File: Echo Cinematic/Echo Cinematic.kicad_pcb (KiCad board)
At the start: 4 copper layers, 57.9 x 111.7 mm, 124 parts, among them J1 IDC, J11 SYM_Arrow45_Tiny, J12 SYM_Arrow45_Tiny, J13 SYM_Arrow45_Tiny, J14 SYM_Arrow45_Tiny, J15 SYM_Arrow45_Tiny, J16 Input R, J2 Play • Rec, J4 Tap • Clock, J5 AUDIO OUT L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

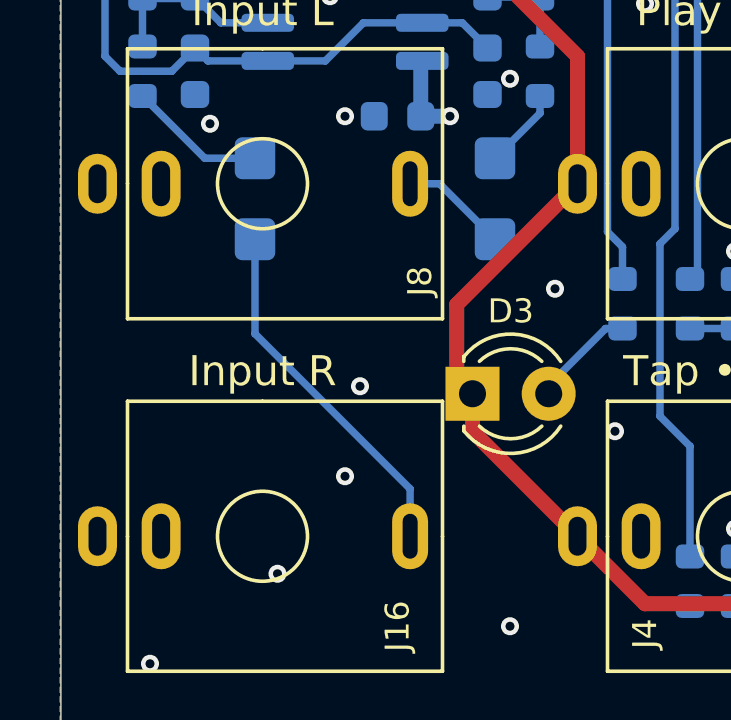
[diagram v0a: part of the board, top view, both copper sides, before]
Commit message: Added input jack switching circuits, fab files updated and finalized.
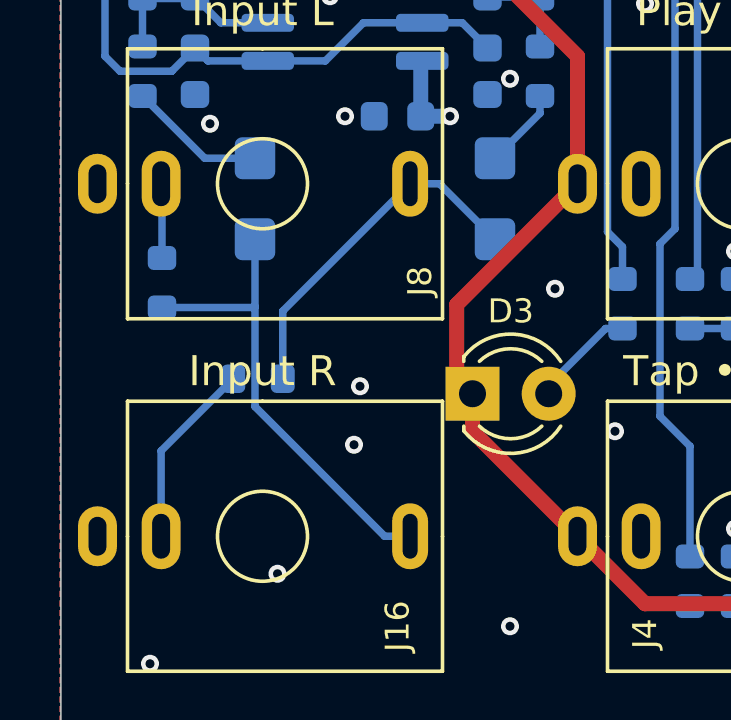
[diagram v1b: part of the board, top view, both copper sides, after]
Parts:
- added R51: 0R, Resistor_SMD:R_0603_1608Metric, B.Cu at (71.6, 137.0)
- added R52: 0R, Resistor_SMD:R_0603_1608Metric, B.Cu at (68.4, 133.8)
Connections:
- J16 pad TN: unconnected-(J16-PadTN) -> Net-(J16-PadTN)
- J8 pad TN: unconnected-(J8-PadTN) -> Net-(J8-PadTN)
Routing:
- net /AUDIO IN/AUDIO_IN_L: track 3.60 -> 11.9 mm
- net Net-(J16-PadTN): track 0.00 -> 6.25 mm
- net /AUDIO IN/AUDIO_IN_R: track 12.0 -> 15.6 mm
- net Net-(J8-PadTN): track 0.00 -> 2.49 mm
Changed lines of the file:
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@@
   (net 58 "unconnected-(J4-PadTN)")
   (net 59 "/AUDIO IN/AUDIO_IN_L")
-  (net 60 "unconnected-(J8-PadTN)")
+  (net 60 "Net-(J8-PadTN)")
   (net 61 "/AUDIO IN/AUDIO_IN_R")
-  (net 62 "unconnected-(J16-PadTN)")
+  (net 62 "Net-(J16-PadTN)")
   (net 63 "Net-(Q2-B)")
   (net 64 "Net-(Q2-C)")
@@
       (net 59 "/AUDIO IN/AUDIO_IN_L") (pintype "passive"))
     (pad "TN" thru_hole oval (at 0 3.38 270) (size 2.2 1.3) (drill oval 1.5 0.6) (layers "*.Cu" "*.Mask")
-      (net 60 "unconnected-(J8-PadTN)") (pintype "passive+no_connect"))
+      (net 60 "Net-(J8-PadTN)") (pintype "passive"))
     (model "${KIPRJMOD}/FOOTPRINTS.pretty/PJ301M-12 Thonkiconn v0.2.stp"
       (offset (xyz 0 0.7 0))
@@
       (net 61 "/AUDIO IN/AUDIO_IN_R") (pintype "passive"))
     (pad "TN" thru_hole oval (at 0 3.38 270) (size 2.2 1.3) (drill oval 1.5 0.6) (layers "*.Cu" "*.Mask")
-      (net 62 "unconnected-(J16-PadTN)") (pintype "passive+no_connect"))
+      (net 62 "Net-(J16-PadTN)") (pintype "passive"))
     (model "${KIPRJMOD}/FOOTPRINTS.pretty/PJ301M-12 Thonkiconn v0.2.stp"
       (offset (xyz 0 0.7 0))
@@
     )
   )
+  (footprint "Resistor_SMD:R_0603_1608Metric" (layer "B.Cu")
+    (at 68.4 133.8 -90)
+    (descr "Resistor SMD 0603 (1608 Metric), square (rectangular) end terminal, IPC_7351 nominal, (Body size source: IPC-SM-782 page 72, https://www.pcb-3d.com/wordpress/wp-content/uploads/ipc-sm-782a_amendment_1_and_2.pdf), generated with kicad-footprint-generator")
+    (tags "resistor")
+    (property "Sheetfile" "AUDIO IN.kicad_sch")
+    (property "Sheetname" "AUDIO IN")
+    (property "ki_description" "Resistor, small symbol")
+    (property "ki_keywords" "R resistor")
+    (attr smd)
+    (fp_text reference "R52" (at 0 1.43 90) (layer "B.SilkS")
+        (effects (font (size 0.8 0.8) (thickness 0.15)) (justify mirror))
+    )
+    (fp_text value "0R" (at 0 -1.43 90) (layer "B.Fab")
+        (effects (font (size 1 1) (thickness 0.15)) (justify mirror))
+    )
+    (fp_text user "${REFERENCE}" (at 0 0 90) (layer "B.Fab")
+        (effects (font (size 0.4 0.4) (thickness 0.06)) (justify mirror))
+    )
+    (fp_line (start -0.237258 -0.5225) (end 0.237258 -0.5225)
+      (stroke (width 0.12) (type solid)) (layer "B.SilkS"))
+    (fp_line (start -0.237258 0.5225) (end 0.237258 0.5225)
+      (stroke (width 0.12) (type solid)) (layer "B.SilkS"))
+    (fp_line (start -1.48 -0.73) (end -1.48 0.73)
+      (stroke (width 0.05) (type solid)) (layer "B.CrtYd"))
+    (fp_line (start -1.48 0.73) (end 1.48 0.73)
+      (stroke (width 0.05) (type solid)) (layer "B.CrtYd"))
+    (fp_line (start 1.48 -0.73) (end -1.48 -0.73)
+      (stroke (width 0.05) (type solid)) (layer "B.CrtYd"))
+    (fp_line (start 1.48 0.73) (end 1.48 -0.73)
+      (stroke (width 0.05) (type solid)) (layer "B.CrtYd"))
+    (fp_line (start -0.8 -0.4125) (end -0.8 0.4125)
+      (stroke (width 0.1) (type solid)) (layer "B.Fab"))
+    (fp_line (start -0.8 0.4125) (end 0.8 0.4125)
+      (stroke (width 0.1) (type solid)) (layer "B.Fab"))
+    (fp_line (start 0.8 -0.4125) (end -0.8 -0.4125)
+      (stroke (width 0.1) (type solid)) (layer "B.Fab"))
+    (fp_line (start 0.8 0.4125) (end 0.8 -0.4125)
+      (stroke (width 0.1) (type solid)) (layer "B.Fab"))
+    (pad "1" smd roundrect (at -0.825 0 270) (size 0.8 0.95) (layers "B.Cu" "B.Paste" "B.Mask") (roundrect_rratio 0.25)
+      (net 60 "Net-(J8-PadTN)") (pintype "passive"))
+    (pad "2" smd roundrect (at 0.825 0 270) (size 0.8 0.95) (layers "B.Cu" "B.Paste" "B.Mask") (roundrect_rratio 0.25)
+      (net 61 "/AUDIO IN/AUDIO_IN_R") (pintype "passive"))
+    (model "${KICAD6_3DMODEL_DIR}/Resistor_SMD.3dshapes/R_0603_1608Metric.wrl"
+      (offset (xyz 0 0 0))
+      (scale (xyz 1 1 1))
+      (rotate (xyz 0 0 0))
+    )
+  )
   (footprint "Capacitor_SMD:C_0603_1608Metric" (layer "B.Cu")
     (at 76.25 128.25 180)
@@
   )
   (footprint "Resistor_SMD:R_0603_1608Metric" (layer "B.Cu")
+    (at 71.6 137 180)
+    (descr "Resistor SMD 0603 (1608 Metric), square (rectangular) end terminal, IPC_7351 nominal, (Body size source: IPC-SM-782 page 72, https://www.pcb-3d.com/wordpress/wp-content/uploads/ipc-sm-782a_amendment_1_and_2.pdf), generated with kicad-footprint-generator")
+    (tags "resistor")
+    (property "Sheetfile" "AUDIO IN.kicad_sch")
+    (property "Sheetname" "AUDIO IN")
+    (property "ki_description" "Resistor, small symbol")
+    (property "ki_keywords" "R resistor")
+    (attr smd)
+    (fp_text reference "R51" (at 0 1.43) (layer "B.SilkS")
+        (effects (font (size 0.8 0.8) (thickness 0.15)) (justify mirror))
+    )
+    (fp_text value "0R" (at 0 -1.43) (layer "B.Fab")
+        (effects (font (size 1 1) (thickness 0.15)) (justify mirror))
+    )
+    (fp_text user "${REFERENCE}" (at 0 0) (layer "B.Fab")
+        (effects (font (size 0.4 0.4) (thickness 0.06)) (justify mirror))
+    )
+    (fp_line (start -0.237258 -0.5225) (end 0.237258 -0.5225)
+      (stroke (width 0.12) (type solid)) (layer "B.SilkS"))
+    (fp_line (start -0.237258 0.5225) (end 0.237258 0.5225)
+      (stroke (width 0.12) (type solid)) (layer "B.SilkS"))
+    (fp_line (start -1.48 -0.73) (end -1.48 0.73)
+      (stroke (width 0.05) (type solid)) (layer "B.CrtYd"))
+    (fp_line (start -1.48 0.73) (end 1.48 0.73)
+      (stroke (width 0.05) (type solid)) (layer "B.CrtYd"))
+    (fp_line (start 1.48 -0.73) (end -1.48 -0.73)
+      (stroke (width 0.05) (type solid)) (layer "B.CrtYd"))
+    (fp_line (start 1.48 0.73) (end 1.48 -0.73)
+      (stroke (width 0.05) (type solid)) (layer "B.CrtYd"))
+    (fp_line (start -0.8 -0.4125) (end -0.8 0.4125)
+      (stroke (width 0.1) (type solid)) (layer "B.Fab"))
+    (fp_line (start -0.8 0.4125) (end 0.8 0.4125)
+      (stroke (width 0.1) (type solid)) (layer "B.Fab"))
+    (fp_line (start 0.8 -0.4125) (end -0.8 -0.4125)
+      (stroke (width 0.1) (type solid)) (layer "B.Fab"))
+    (fp_line (start 0.8 0.4125) (end 0.8 -0.4125)
+      (stroke (width 0.1) (type solid)) (layer "B.Fab"))
+    (pad "1" smd roundrect (at -0.825 0 180) (size 0.8 0.95) (layers "B.Cu" "B.Paste" "B.Mask") (roundrect_rratio 0.25)
+      (net 59 "/AUDIO IN/AUDIO_IN_L") (pintype "passive"))
+    (pad "2" smd roundrect (at 0.825 0 180) (size 0.8 0.95) (layers "B.Cu" "B.Paste" "B.Mask") (roundrect_rratio 0.25)
+      (net 62 "Net-(J16-PadTN)") (pintype "passive"))
+    (model "${KICAD6_3DMODEL_DIR}/Resistor_SMD.3dshapes/R_0603_1608Metric.wrl"
+      (offset (xyz 0 0 0))
+      (scale (xyz 1 1 1))
+      (rotate (xyz 0 0 0))
+    )
+  )
+  (footprint "Resistor_SMD:R_0603_1608Metric" (layer "B.Cu")
     (at 86 143.75 90)
     (descr "Resistor SMD 0603 (1608 Metric), square (rectangular) end terminal, IPC_7351 nominal, (Body size source: IPC-SM-782 page 72, https://www.pcb-3d.com/wordpress/wp-content/uploads/ipc-sm-782a_amendment_1_and_2.pdf), generated with kicad-footprint-generator")
@@
   (via (at 121.5 128) (size 0.6) (drill 0.3) (layers "F.Cu" "B.Cu") (free) (net 4))
   (via (at 107.5 136) (size 0.6) (drill 0.3) (layers "F.Cu" "B.Cu") (free) (net 4))
-  (via (at 74.5 140.25) (size 0.6) (drill 0.3) (layers "F.Cu" "B.Cu") (free) (net 4))
+  (via (at 74.8 139.2) (size 0.6) (drill 0.3) (layers "F.Cu" "B.Cu") (free) (net 4))
   (via (at 92.5 92) (size 0.6) (drill 0.3) (layers "F.Cu" "B.Cu") (free) (net 4))
   (via (at 68 146.5) (size 0.6) (drill 0.3) (layers "F.Cu" "B.Cu") (free) (net 4))
@@
   (segment (start 92.67 140.595) (end 90.825 138.75) (width 0.25) (layer "B.Cu") (net 57))
   (segment (start 92.67 142.25) (end 92.67 140.595) (width 0.25) (layer "B.Cu") (net 57))
+  (segment (start 72.425 134.745) (end 76.67 130.5) (width 0.25) (layer "B.Cu") (net 59))
   (segment (start 76.67 130.5) (end 77.65 130.5) (width 0.25) (layer "B.Cu") (net 59))
+  (segment (start 72.425 137) (end 72.425 134.745) (width 0.25) (layer "B.Cu") (net 59))
   (segment (start 77.65 130.5) (end 79.5 132.35) (width 0.25) (layer "B.Cu") (net 59))
-  (segment (start 71.5 135.5) (end 76.67 140.67) (width 0.25) (layer "B.Cu") (net 61))
-  (segment (start 71.5 132.35) (end 71.5 135.5) (width 0.25) (layer "B.Cu") (net 61))
-  (segment (start 76.67 140.67) (end 76.67 142.25) (width 0.25) (layer "B.Cu") (net 61))
+  (segment (start 68.4 132.975) (end 68.4 130.53) (width 0.25) (layer "B.Cu") (net 60))
+  (segment (start 68.4 130.53) (end 68.37 130.5) (width 0.25) (layer "B.Cu") (net 60))
+  (segment (start 68.4 134.625) (end 71.475 134.625) (width 0.25) (layer "B.Cu") (net 61))
+  (segment (start 71.5 137.93) (end 71.5 134.6) (width 0.25) (layer "B.Cu") (net 61))
+  (segment (start 76.67 142.25) (end 75.82 142.25) (width 0.25) (layer "B.Cu") (net 61))
+  (segment (start 71.5 134.6) (end 71.5 132.35) (width 0.25) (layer "B.Cu") (net 61))
+  (segment (start 71.475 134.625) (end 71.5 134.6) (width 0.25) (layer "B.Cu") (net 61))
+  (segment (start 75.82 142.25) (end 71.5 137.93) (width 0.25) (layer "B.Cu") (net 61))
+  (segment (start 68.37 142.25) (end 68.37 139.405) (width 0.25) (layer "B.Cu") (net 62))
+  (segment (start 68.37 139.405) (end 70.775 137) (width 0.25) (layer "B.Cu") (net 62))
   (segment (start 89.175 138.75) (end 89.175 140.5) (width 0.25) (layer "B.Cu") (net 63))
   (segment (start 89.05 142.5625) (end 89.05 140.625) (width 0.25) (layer "B.Cu") (net 63))
